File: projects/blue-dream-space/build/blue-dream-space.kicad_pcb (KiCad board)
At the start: 4 copper layers, 347.5 x 137 mm, 269 parts, among them J1 USB_C, SW1 SW_Push, SW10 SW_Push, SW11 SW_Push, SW12 SW_Push, SW13 SW_Push, SW14 SW_Push, SW15 SW_Push, SW16 SW_Push, SW17 SW_Push, SW18 SW_Push, SW19 SW_Push, SW2 SW_Push, SW20 SW_Push, SW21 SW_Push, SW22 SW_Push, SW23 SW_Push, SW24 SW_Push, SW25 SW_Push, SW26 SW_Push, SW27 SW_Push, SW28 SW_Push, SW29 SW_Push, SW3 SW_Push, SW30 SW_Push, SW31 SW_Push, SW32 SW_Push, SW33 SW_Push, SW34 SW_Push, SW35 SW_Push, SW36 SW_Push, SW37 SW_Push, SW38 SW_Push, SW39 SW_Push, SW4 SW_Push, SW40 SW_Push, SW41 SW_Push, SW42 SW_Push, SW43 SW_Push, SW44 SW_Push, SW45 SW_Push, SW46 SW_Push, SW47 SW_Push, SW48 SW_Push, SW49 SW_Push, SW5 SW_Push, SW50 SW_Push, SW51 SW_Push, SW52 SW_Push, SW53 SW_Push, SW54 SW_Push, SW55 SW_Push, SW56 SW_Push, SW57 SW_Push, SW58 SW_Push, SW59 SW_Push, SW6 SW_Push, SW60 SW_Push, SW61 SW_Push, SW62 SW_Push, SW63 SW_Push, SW64 SW_Push, SW65 SW_Push, SW66 SW_Push, SW67 SW_Push, SW68 SW_Push, SW69 SW_Push, SW7 SW_Push, SW70 SW_Push, SW71 SW_Push, SW72 SW_Push, SW73 SW_Push, SW74 SW_Push, SW75 SW_Push, SW76 SW_Push, SW77 SW_Push, SW78 SW_Push, SW79 SW_Push, SW8 SW_Push, SW80 SW_Push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

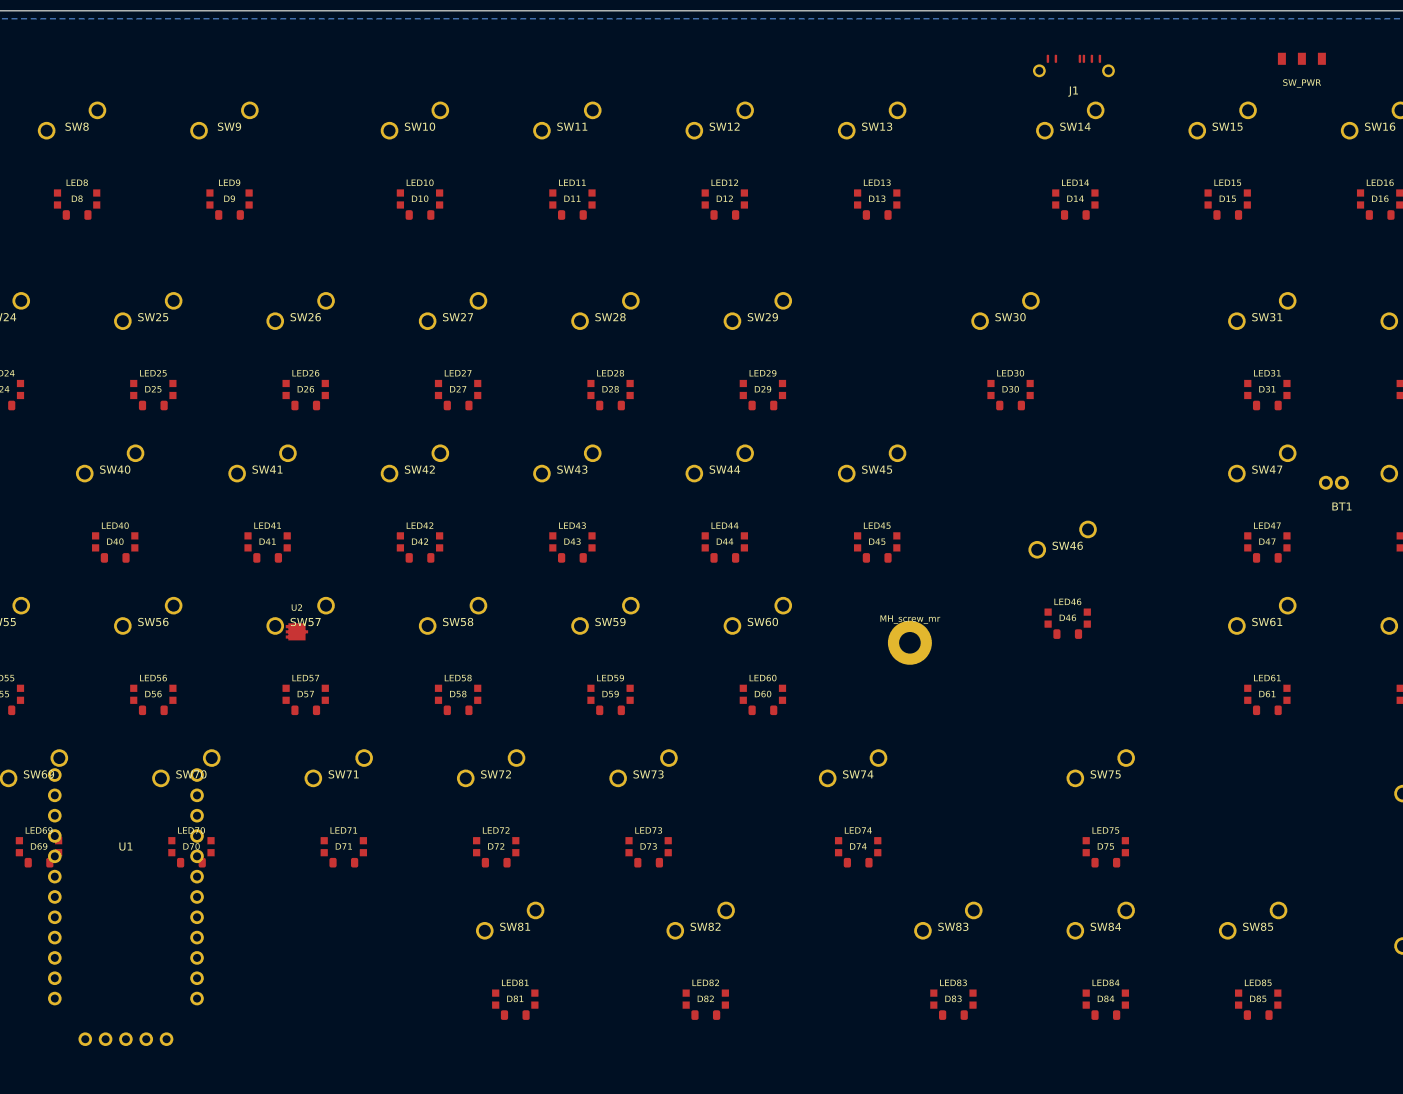
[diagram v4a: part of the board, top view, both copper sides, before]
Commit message: refactor: design tokens, shared primitives, and architecture decomposition
Design system & styling (Phase A):
- Extend global.css with spacing/font/transition/z-index/chrome tokens
- Add success-soft, warning-soft, error-soft, accent-soft, border-strong colors
- Replace ~62 hardcoded hex colors across views with design tokens
- Apply transition duration tokens to components.css and shell.css
- Add utility classes (u-stack, u-text-muted, panel-heading, field-label, empty-state)
- Global *:focus-visible accent outline for keyboard users
- Global accent-color for native checkboxes/radios
- Toast container offset uses calc(--status-bar-height + space)
- Document CSS naming convention at top of global.css
- New utils/format.ts with formatBytes/formatDuration/formatDateTime/formatRelativeTime
- FileLink and Build.tsx migrated to shared format helpers
- LayoutEditor uses panel-heading class instead of duplicated inline styles

Shared primitives (Phase B):
- New Input component (label, hint, error, sizes, prefix/suffix, onEnter)
- New Checkbox component (label, description slot, sizes, switch variant)
- New EmptyState component (icon, title, message, actions, variants)
- Modal accepts size prop (sm/md/lg/xl) + scroll-shadow + aria + hideClose
- NewProject migrated to Input with hint/error states
- Build.tsx routing settings + output checkboxes use Input + Checkbox
- Overview/Build empty states use EmptyState

Theme infrastructure (Phase B):
- Light theme tokens defined under [data-theme="light"]
- prefers-color-scheme: light auto-activates when no override
- index.html pins data-theme="dark" preserving current appearance

Server helpers (Phase B):
- New server/utils/safe-path.ts with centralized path-traversal protection
- build.routes.ts file serving migrated to safePath()

Type safety (Phase B):
- New src/wizard/src/types/mcu.types.ts mirroring tools package types
- LayoutState ComponentDataSet replaces any with McuData/ComponentOption
- getMcuDimensions strongly typed
- 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
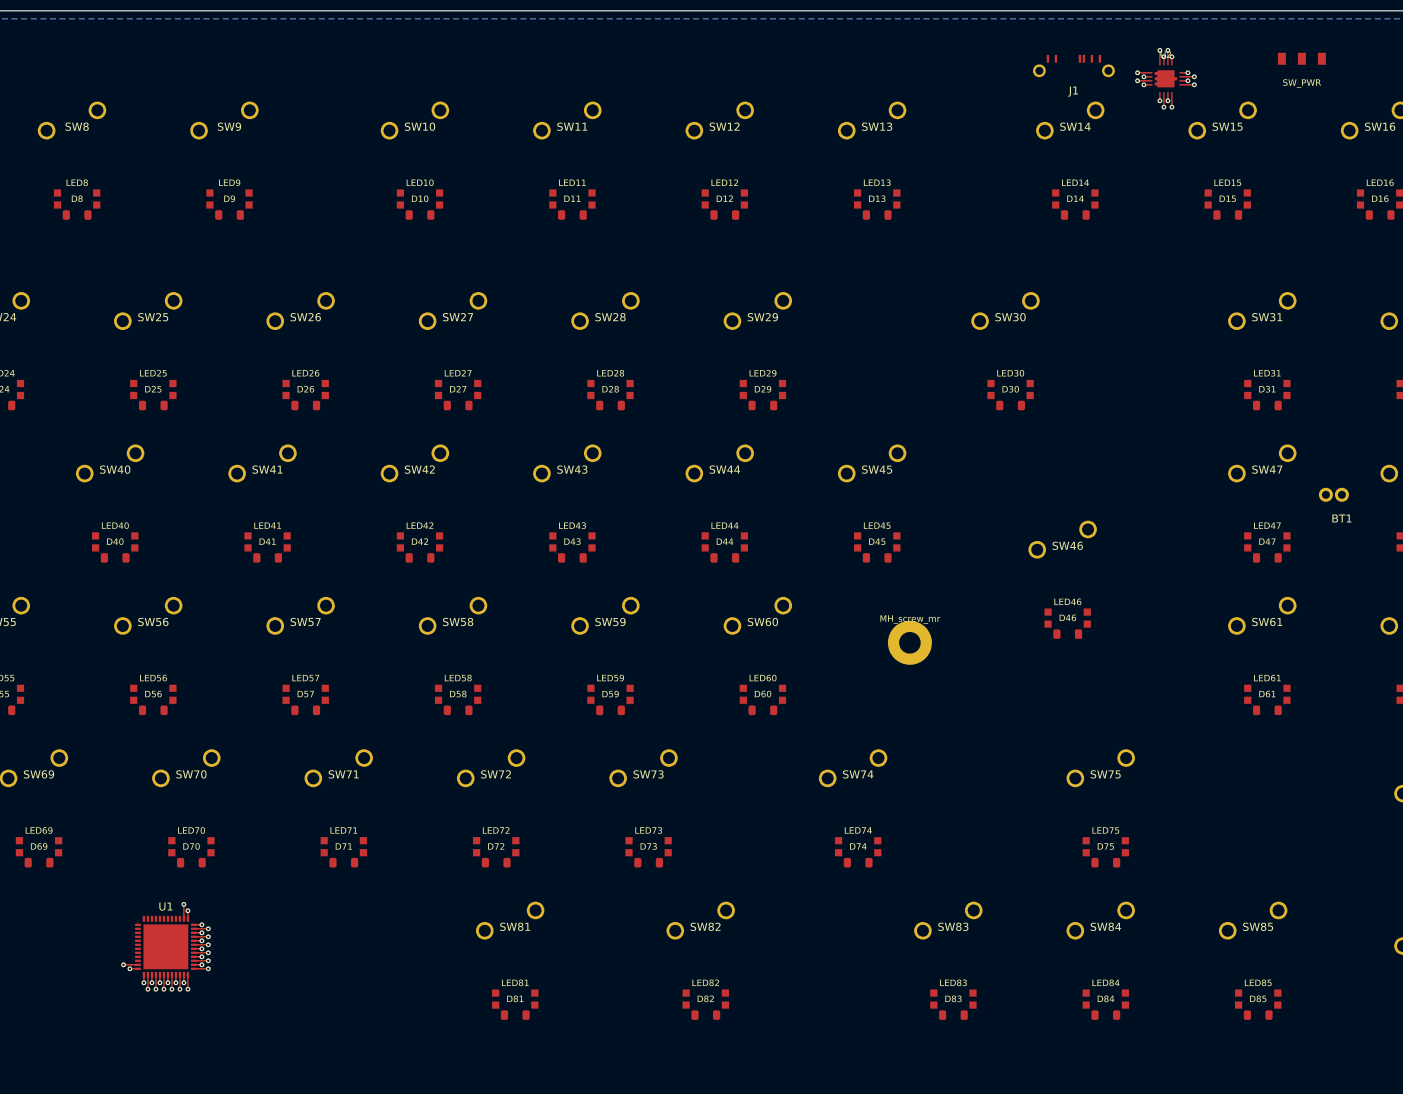
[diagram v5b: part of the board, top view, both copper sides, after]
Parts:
- U1: value nice!nano v2 -> STM32WB55; footprint Module:pro-micro_29pin_P2.54mm -> Package_DFN_QFN:QFN-48-1EP_7x7mm_P0.5mm_EP5.6x5.6mm
- moved U2 128.8 mm to (313.5, 25.5)
- moved U1 9.01 mm to (188.5, 134.0)
- moved BT1 1.50 mm to (335.5, 77.5)
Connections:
- D10 pad 1: ROW1 -> ROW0
- D10 pad 2: COL1 -> COL9
- D11 pad 1: ROW1 -> ROW0
- D11 pad 2: COL2 -> COL10
- D12 pad 1: ROW1 -> ROW0
- D12 pad 2: COL3 -> COL11
- D13 pad 1: ROW1 -> ROW0
- D13 pad 2: COL4 -> COL12
- D14 pad 1: ROW1 -> ROW0
- D14 pad 2: COL5 -> COL13
- D15 pad 1: ROW1 -> ROW0
- D15 pad 2: COL6 -> COL14
- D16 pad 1: ROW1 -> ROW0
- D16 pad 2: COL7 -> COL15
- D17 pad 1: ROW2 -> ROW1
- D18 pad 1: ROW2 -> ROW1
- D19 pad 1: ROW2 -> ROW1
- D20 pad 1: ROW2 -> ROW1
- D21 pad 1: ROW2 -> ROW1
- D22 pad 1: ROW2 -> ROW1
- D23 pad 1: ROW2 -> ROW1
- D24 pad 1: ROW2 -> ROW1
- D25 pad 1: ROW3 -> ROW1
- D25 pad 2: COL0 -> COL8
- D26 pad 1: ROW3 -> ROW1
- D26 pad 2: COL1 -> COL9
- D27 pad 1: ROW3 -> ROW1
- D27 pad 2: COL2 -> COL10
- D28 pad 1: ROW3 -> ROW1
- D28 pad 2: COL3 -> COL11
- D29 pad 1: ROW3 -> ROW1
- D29 pad 2: COL4 -> COL12
- D30 pad 1: ROW3 -> ROW1
- D30 pad 2: COL5 -> COL13
- D31 pad 1: ROW3 -> ROW1
- D31 pad 2: COL6 -> COL14
- D32 pad 1: ROW3 -> ROW1
- D32 pad 2: COL7 -> COL15
- D33 pad 1: ROW4 -> ROW2
- D34 pad 1: ROW4 -> ROW2
- D35 pad 1: ROW4 -> ROW2
- D36 pad 1: ROW4 -> ROW2
- D37 pad 1: ROW4 -> ROW2
- D38 pad 1: ROW4 -> ROW2
- D39 pad 1: ROW4 -> ROW2
- D40 pad 1: ROW4 -> ROW2
- D41 pad 1: ROW5 -> ROW2
- D41 pad 2: COL0 -> COL8
- D42 pad 1: ROW5 -> ROW2
- D42 pad 2: COL1 -> COL9
- D43 pad 1: ROW5 -> ROW2
- D43 pad 2: COL2 -> COL10
- D44 pad 1: ROW5 -> ROW2
- D44 pad 2: COL3 -> COL11
- D45 pad 1: ROW5 -> ROW2
- D45 pad 2: COL4 -> COL12
- D46 pad 1: ROW5 -> ROW2
- D46 pad 2: COL5 -> COL13
- D47 pad 1: ROW5 -> ROW2
- D47 pad 2: COL6 -> COL14
- D48 pad 1: ROW5 -> ROW2
- D48 pad 2: COL7 -> COL15
- D49 pad 1: ROW6 -> ROW3
- D50 pad 1: ROW6 -> ROW3
- D51 pad 1: ROW6 -> ROW3
- D52 pad 1: ROW6 -> ROW3
- D53 pad 1: ROW6 -> ROW3
- D54 pad 1: ROW6 -> ROW3
- D55 pad 1: ROW6 -> ROW3
- D56 pad 1: ROW7 -> ROW3
- D56 pad 2: COL0 -> COL7
- D57 pad 1: ROW7 -> ROW3
- D57 pad 2: COL1 -> COL8
- D58 pad 1: ROW7 -> ROW3
- D58 pad 2: COL2 -> COL9
- D59 pad 1: ROW7 -> ROW3
- D59 pad 2: COL3 -> COL10
- D60 pad 1: ROW7 -> ROW3
- D60 pad 2: COL4 -> COL11
- D61 pad 1: ROW7 -> ROW3
- D61 pad 2: COL5 -> COL12
- D62 pad 1: ROW7 -> ROW3
- D62 pad 2: COL6 -> COL13
- D63 pad 1: ROW8 -> ROW4
- D64 pad 1: ROW8 -> ROW4
- D65 pad 1: ROW8 -> ROW4
- D66 pad 1: ROW8 -> ROW4
- D67 pad 1: ROW8 -> ROW4
- D68 pad 1: ROW8 -> ROW4
- D69 pad 1: ROW8 -> ROW4
- D70 pad 1: ROW9 -> ROW4
- D70 pad 2: COL0 -> COL7
- D71 pad 1: ROW9 -> ROW4
- D71 pad 2: COL1 -> COL8
- D72 pad 1: ROW9 -> ROW4
- D72 pad 2: COL2 -> COL9
- D73 pad 1: ROW9 -> ROW4
- D73 pad 2: COL3 -> COL10
- D74 pad 1: ROW9 -> ROW4
- D74 pad 2: COL4 -> COL11
- D75 pad 1: ROW9 -> ROW4
- D75 pad 2: COL5 -> COL12
- D76 pad 1: ROW9 -> ROW4
- D76 pad 2: COL6 -> COL13
- D77 pad 1: ROW10 -> ROW5
- D78 pad 1: ROW10 -> ROW5
- D79 pad 1: ROW10 -> ROW5
- D80 pad 1: ROW10 -> ROW5
- D81 pad 1: ROW10 -> ROW5
- D82 pad 1: ROW10 -> ROW5
- D83 pad 1: ROW10 -> ROW5
- D84 pad 1: ROW10 -> ROW5
- D85 pad 1: ROW10 -> ROW5
- D86 pad 1: ROW10 -> ROW5
- D9 pad 1: ROW1 -> ROW0
- D9 pad 2: COL0 -> COL8
- SW10 pad 1: COL1 -> COL9
- SW10 pad 2: ROW1 -> ROW0
- SW11 pad 1: COL2 -> COL10
- SW11 pad 2: ROW1 -> ROW0
- SW12 pad 1: COL3 -> COL11
- SW12 pad 2: ROW1 -> ROW0
- SW13 pad 1: COL4 -> COL12
- SW13 pad 2: ROW1 -> ROW0
- SW14 pad 1: COL5 -> COL13
- SW14 pad 2: ROW1 -> ROW0
- SW15 pad 1: COL6 -> COL14
- SW15 pad 2: ROW1 -> ROW0
- SW16 pad 1: COL7 -> COL15
- SW16 pad 2: ROW1 -> ROW0
- SW17 pad 2: ROW2 -> ROW1
- SW18 pad 2: ROW2 -> ROW1
- SW19 pad 2: ROW2 -> ROW1
- SW20 pad 2: ROW2 -> ROW1
- SW21 pad 2: ROW2 -> ROW1
- SW22 pad 2: ROW2 -> ROW1
- SW23 pad 2: ROW2 -> ROW1
- SW24 pad 2: ROW2 -> ROW1
- SW25 pad 1: COL0 -> COL8
- SW25 pad 2: ROW3 -> ROW1
- SW26 pad 1: COL1 -> COL9
- SW26 pad 2: ROW3 -> ROW1
- SW27 pad 1: COL2 -> COL10
- SW27 pad 2: ROW3 -> ROW1
- SW28 pad 1: COL3 -> COL11
- SW28 pad 2: ROW3 -> ROW1
- SW29 pad 1: COL4 -> COL12
- SW29 pad 2: ROW3 -> ROW1
- SW30 pad 1: COL5 -> COL13
- SW30 pad 2: ROW3 -> ROW1
- SW31 pad 1: COL6 -> COL14
- SW31 pad 2: ROW3 -> ROW1
- SW32 pad 1: COL7 -> COL15
- SW32 pad 2: ROW3 -> ROW1
- SW33 pad 2: ROW4 -> ROW2
- SW34 pad 2: ROW4 -> ROW2
- SW35 pad 2: ROW4 -> ROW2
- SW36 pad 2: ROW4 -> ROW2
- SW37 pad 2: ROW4 -> ROW2
- SW38 pad 2: ROW4 -> ROW2
- SW39 pad 2: ROW4 -> ROW2
- SW40 pad 2: ROW4 -> ROW2
- SW41 pad 1: COL0 -> COL8
- SW41 pad 2: ROW5 -> ROW2
- SW42 pad 1: COL1 -> COL9
- SW42 pad 2: ROW5 -> ROW2
- SW43 pad 1: COL2 -> COL10
- SW43 pad 2: ROW5 -> ROW2
- SW44 pad 1: COL3 -> COL11
- SW44 pad 2: ROW5 -> ROW2
- SW45 pad 1: COL4 -> COL12
- SW45 pad 2: ROW5 -> ROW2
- SW46 pad 1: COL5 -> COL13
- SW46 pad 2: ROW5 -> ROW2
- SW47 pad 1: COL6 -> COL14
- SW47 pad 2: ROW5 -> ROW2
- SW48 pad 1: COL7 -> COL15
- SW48 pad 2: ROW5 -> ROW2
- SW49 pad 2: ROW6 -> ROW3
- SW50 pad 2: ROW6 -> ROW3
- SW51 pad 2: ROW6 -> ROW3
- SW52 pad 2: ROW6 -> ROW3
- SW53 pad 2: ROW6 -> ROW3
- SW54 pad 2: ROW6 -> ROW3
- SW55 pad 2: ROW6 -> ROW3
- SW56 pad 1: COL0 -> COL7
- SW56 pad 2: ROW7 -> ROW3
- SW57 pad 1: COL1 -> COL8
- SW57 pad 2: ROW7 -> ROW3
- SW58 pad 1: COL2 -> COL9
- SW58 pad 2: ROW7 -> ROW3
- SW59 pad 1: COL3 -> COL10
- SW59 pad 2: ROW7 -> ROW3
- SW60 pad 1: COL4 -> COL11
- SW60 pad 2: ROW7 -> ROW3
- SW61 pad 1: COL5 -> COL12
- SW61 pad 2: ROW7 -> ROW3
- SW62 pad 1: COL6 -> COL13
- SW62 pad 2: ROW7 -> ROW3
- SW63 pad 2: ROW8 -> ROW4
- SW64 pad 2: ROW8 -> ROW4
- SW65 pad 2: ROW8 -> ROW4
- SW66 pad 2: ROW8 -> ROW4
- SW67 pad 2: ROW8 -> ROW4
- SW68 pad 2: ROW8 -> ROW4
- SW69 pad 2: ROW8 -> ROW4
- SW70 pad 1: COL0 -> COL7
- SW70 pad 2: ROW9 -> ROW4
- SW71 pad 1: COL1 -> COL8
- SW71 pad 2: ROW9 -> ROW4
- SW72 pad 1: COL2 -> COL9
- SW72 pad 2: ROW9 -> ROW4
- SW73 pad 1: COL3 -> COL10
- SW73 pad 2: ROW9 -> ROW4
- SW74 pad 1: COL4 -> COL11
- SW74 pad 2: ROW9 -> ROW4
- SW75 pad 1: COL5 -> COL12
- SW75 pad 2: ROW9 -> ROW4
- SW76 pad 1: COL6 -> COL13
- SW76 pad 2: ROW9 -> ROW4
- SW77 pad 2: ROW10 -> ROW5
- SW78 pad 2: ROW10 -> ROW5
- SW79 pad 2: ROW10 -> ROW5
- SW80 pad 2: ROW10 -> ROW5
- SW81 pad 2: ROW10 -> ROW5
- SW82 pad 2: ROW10 -> ROW5
- SW83 pad 2: ROW10 -> ROW5
- SW84 pad 2: ROW10 -> ROW5
- SW85 pad 2: ROW10 -> ROW5
- SW86 pad 2: ROW10 -> ROW5
- SW9 pad 1: COL0 -> COL8
- SW9 pad 2: ROW1 -> ROW0
- U1 pad 1: VBAT -> ROW0
- U1 pad 10: ROW5 -> USB_DP
- U1 pad 11: ROW6 -> USB_DM
- U1 pad 12: ROW7 -> COL3
- U1 pad 13: VBUS -> COL4
- U1 pad 15: (no net) -> VCC
- U1 pad 16: VCC -> COL5
- U1 pad 17: ROW8 -> COL6
- U1 pad 18: ROW9 -> COL7
- U1 pad 19: ROW10 -> COL8
- U1 pad 2: GND -> ROW1
- U1 pad 20: COL0 -> COL9
- U1 pad 21: COL1 -> COL10
- U1 pad 22: COL2 -> COL11
- U1 pad 23: COL3 -> COL12
- U1 pad 24: COL4 -> COL13
- U1 pad 25: COL5 -> COL14
- U1 pad 26: COL6 -> COL15
- U1 pad 27: COL7 -> (no net)
- U1 pad 28: COL8 -> (no net)
- U1 pad 29: COL9 -> (no net)
- U1 pad 3: (no net) -> ROW2
- U1 pad 4: VCC -> ROW3
- U1 pad 5: ROW0 -> ROW4
- U1 pad 6: ROW1 -> ROW5
- U1 pad 7: ROW2 -> COL0
- U1 pad 8: ROW3 -> COL1
- U1 pad 9: ROW4 -> COL2
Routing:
- net VCC: track 0.00 -> 10.0 mm, vias 0 -> 6
- net GND: track 0.00 -> 10.0 mm, vias 0 -> 6
- net VBUS: track 0.00 -> 4.00 mm, vias 0 -> 4
- net VBAT: track 0.00 -> 4.00 mm, vias 0 -> 4
- net USB_DP: track 0.00 -> 1.80 mm, vias 0 -> 1
- net ROW5: track 0.00 -> 1.80 mm, vias 0 -> 1
- net ROW3: track 0.00 -> 1.80 mm, vias 0 -> 1
- net ROW1: track 0.00 -> 1.80 mm, vias 0 -> 1
- net COL9: track 0.00 -> 1.80 mm, vias 0 -> 1
- net COL7: track 0.00 -> 1.80 mm, vias 0 -> 1
- net COL5: track 0.00 -> 1.80 mm, vias 0 -> 1
- net COL3: track 0.00 -> 1.80 mm, vias 0 -> 1
- net COL15: track 0.00 -> 1.80 mm, vias 0 -> 1
- net COL13: track 0.00 -> 1.80 mm, vias 0 -> 1
- net COL11: track 0.00 -> 1.80 mm, vias 0 -> 1
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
